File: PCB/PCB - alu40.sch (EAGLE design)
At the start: 163 parts, among them IC1 XB3303ASOT23, IC2 TP4054-42-SOT25-R, J1 SK-3296S-01-L1, J2 USB4510-03-1-A, Q2 PMOSFET, Q3 PMOSFET, Q5 PMOSFET, Q6 NMOSFET, U1 ISP1807-LRISP1807-LR_ISP1807-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, X1 BM02B-SRSS-TB

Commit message: Move reset switch
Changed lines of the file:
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@@
 <pinref part="U1" gate="A" pin="P0.12"/>
 <wire x1="-182.88" y1="-76.2" x2="-182.88" y2="-78.74" width="0.1524" layer="91"/>
-<label x="-182.88" y="-78.74" size="1.778" layer="95" rot="R180"/>
+<label x="-182.88" y="-78.74" size="1.778" layer="95" rot="R270"/>
 </segment>
 </net>

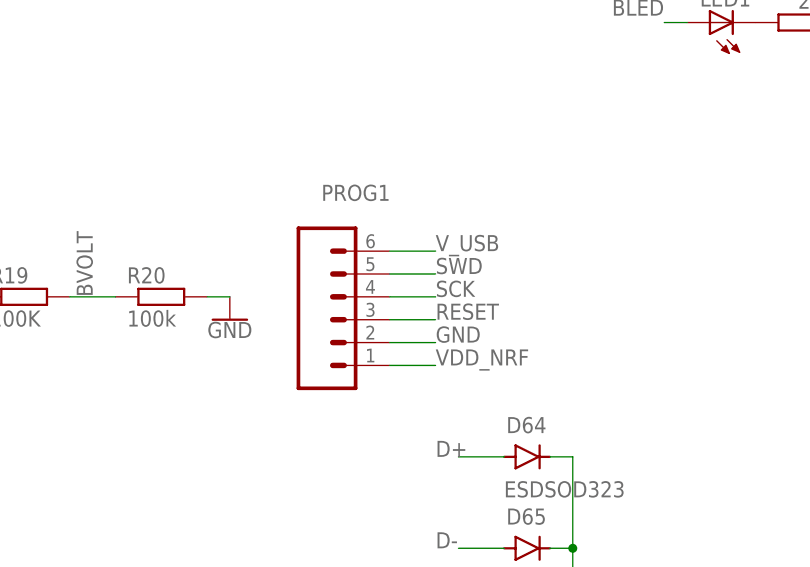
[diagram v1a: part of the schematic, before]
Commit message: Remove unnecessary swd pin
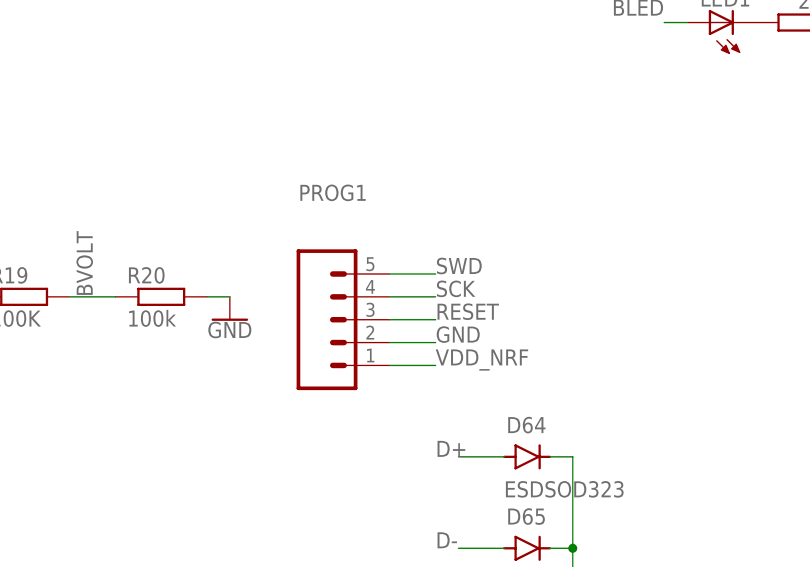
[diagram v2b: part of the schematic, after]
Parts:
- PROG1: device SparkFun-Connectors:CONN_061.27MM -> SparkFun-Connectors:CONN_051.27MM
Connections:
- net V_USB: no longer PROG1.6
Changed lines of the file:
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@@
 <part name="GND31" library="SparkFun-PowerSymbols" library_urn="urn:adsk.eagle:library:530" deviceset="GND" device=""/>
 <part name="SUPPLY17" library="SparkFun-PowerSymbols" library_urn="urn:adsk.eagle:library:530" deviceset="V_BATT" device=""/>
-<part name="PROG1" library="SparkFun-Connectors" library_urn="urn:adsk.eagle:library:513" deviceset="CONN_06" device="1.27MM" package3d_urn="urn:adsk.eagle:package:38131/1"/>
+<part name="PROG1" library="SparkFun-Connectors" library_urn="urn:adsk.eagle:library:513" deviceset="CONN_05" device="1.27MM" package3d_urn="urn:adsk.eagle:package:38110/1"/>
 <part name="LED1" library="adafruit" library_urn="urn:adsk.eagle:library:420" deviceset="LED" device="CHIPLED_0805" package3d_urn="urn:adsk.eagle:package:6240559/1"/>
 <part name="R1" library="rcl" library_urn="urn:adsk.eagle:library:334" deviceset="R-EU_" device="R0603" package3d_urn="urn:adsk.eagle:package:23555/3" value="200"/>
@@
 <attribute name="VALUE" x="-381" y="-40.386" size="1.778" layer="96" align="bottom-center"/>
 </instance>
-<instance part="PROG1" gate="G$1" x="-337.82" y="-45.72" smashed="yes">
-<attribute name="VALUE" x="-340.36" y="-55.626" size="1.778" layer="96" font="vector"/>
-<attribute name="NAME" x="-340.36" y="-32.512" size="1.778" layer="95" font="vector"/>
+<instance part="PROG1" gate="G$1" x="-340.36" y="-45.72" smashed="yes">
+<attribute name="VALUE" x="-342.9" y="-55.626" size="1.778" layer="96" font="vector"/>
+<attribute name="NAME" x="-342.9" y="-32.512" size="1.778" layer="95" font="vector"/>
 </instance>
 <instance part="LED1" gate="G$1" x="-297.18" y="-12.7" smashed="yes" rot="R90">
@@
 </segment>
 <segment>
-<pinref part="PROG1" gate="G$1" pin="6"/>
-<wire x1="-332.74" y1="-38.1" x2="-327.66" y2="-38.1" width="0.1524" layer="91"/>
-<label x="-327.66" y="-38.1" size="1.778" layer="95"/>
-</segment>
-<segment>

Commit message: add silk, spare diodes, move D1
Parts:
- added D49, D50, D51, D52: 1N4148WS, Volume_V1:1N4148WS
